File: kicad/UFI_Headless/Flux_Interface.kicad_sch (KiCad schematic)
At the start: 14 parts, among them U6 SN74LS07D, U7 SN74LS07D, U8 74LVC14AD

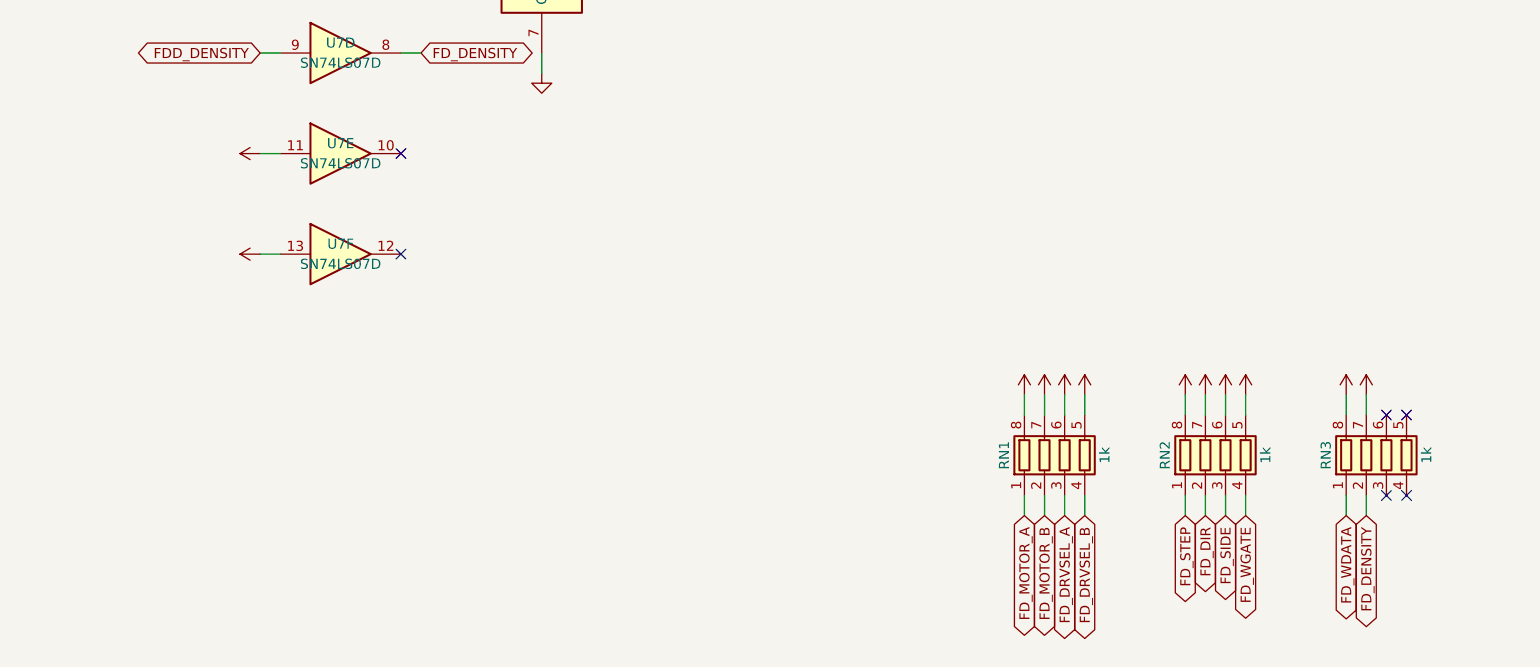
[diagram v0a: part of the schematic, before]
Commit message: UFI Headless v0.4: J6 pin 6 DRATE via JP1, pin 3 GND/+5V via JP2
DRATE is driven by PF11 through the spare LS07 gate U7.11 -> U7.10 with
pull-up RN3.3; J6 pin 6 only sees it when solder jumper JP1 is bridged.
J6 pin 3 goes through JP2 (default 1-2 = GND, 2-3 = FDD_5V for PS/2 drives).
Firmware moves FDD_DRATE from PE6 to PF11.
DRC 0 violations, 0 unconnected, parity clean; fab outputs regenerated.
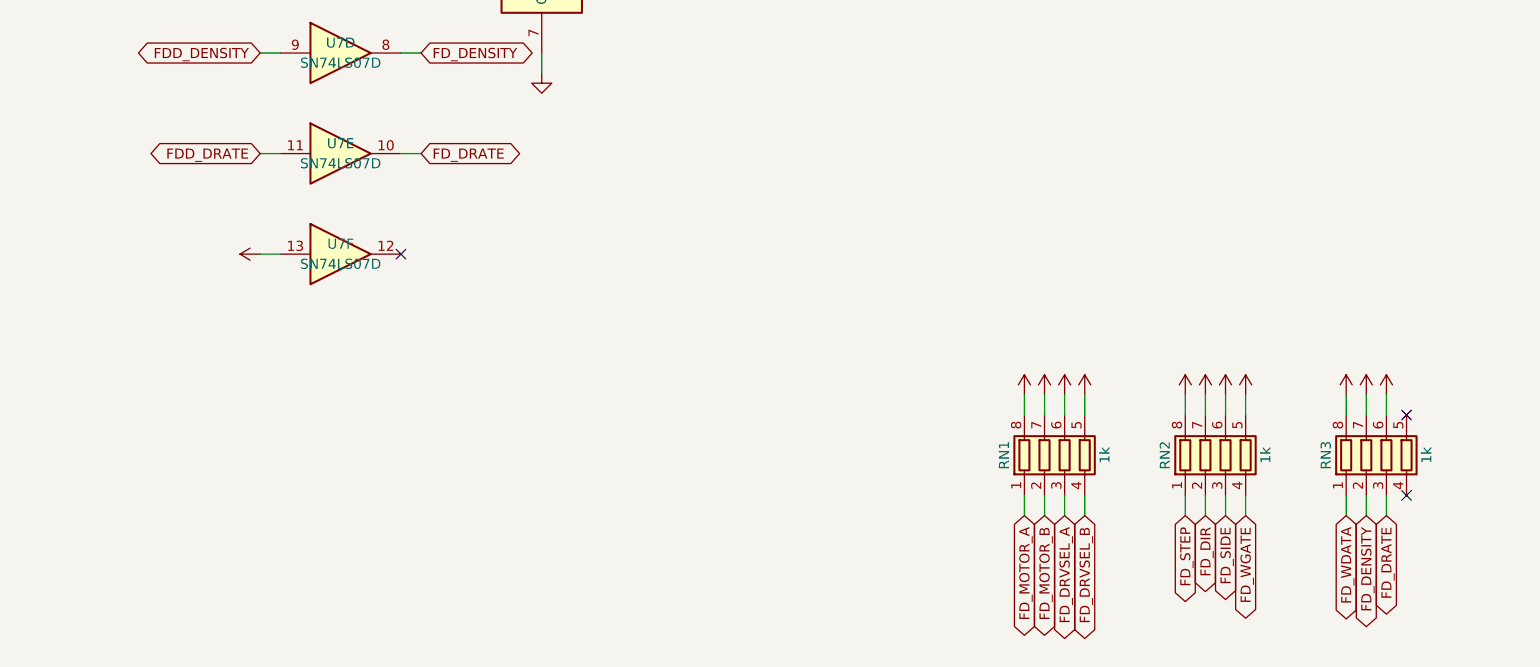
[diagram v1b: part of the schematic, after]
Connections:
- net +5V: now also RN3.6 (R3.2); no longer U7.11
- net FD_DRATE: now reaches RN3.3 (R3.1)
- net FD_DRATE: now also U7.10
- new net FDD_DRATE: U7.11
- no-connect marks 10 -> 7

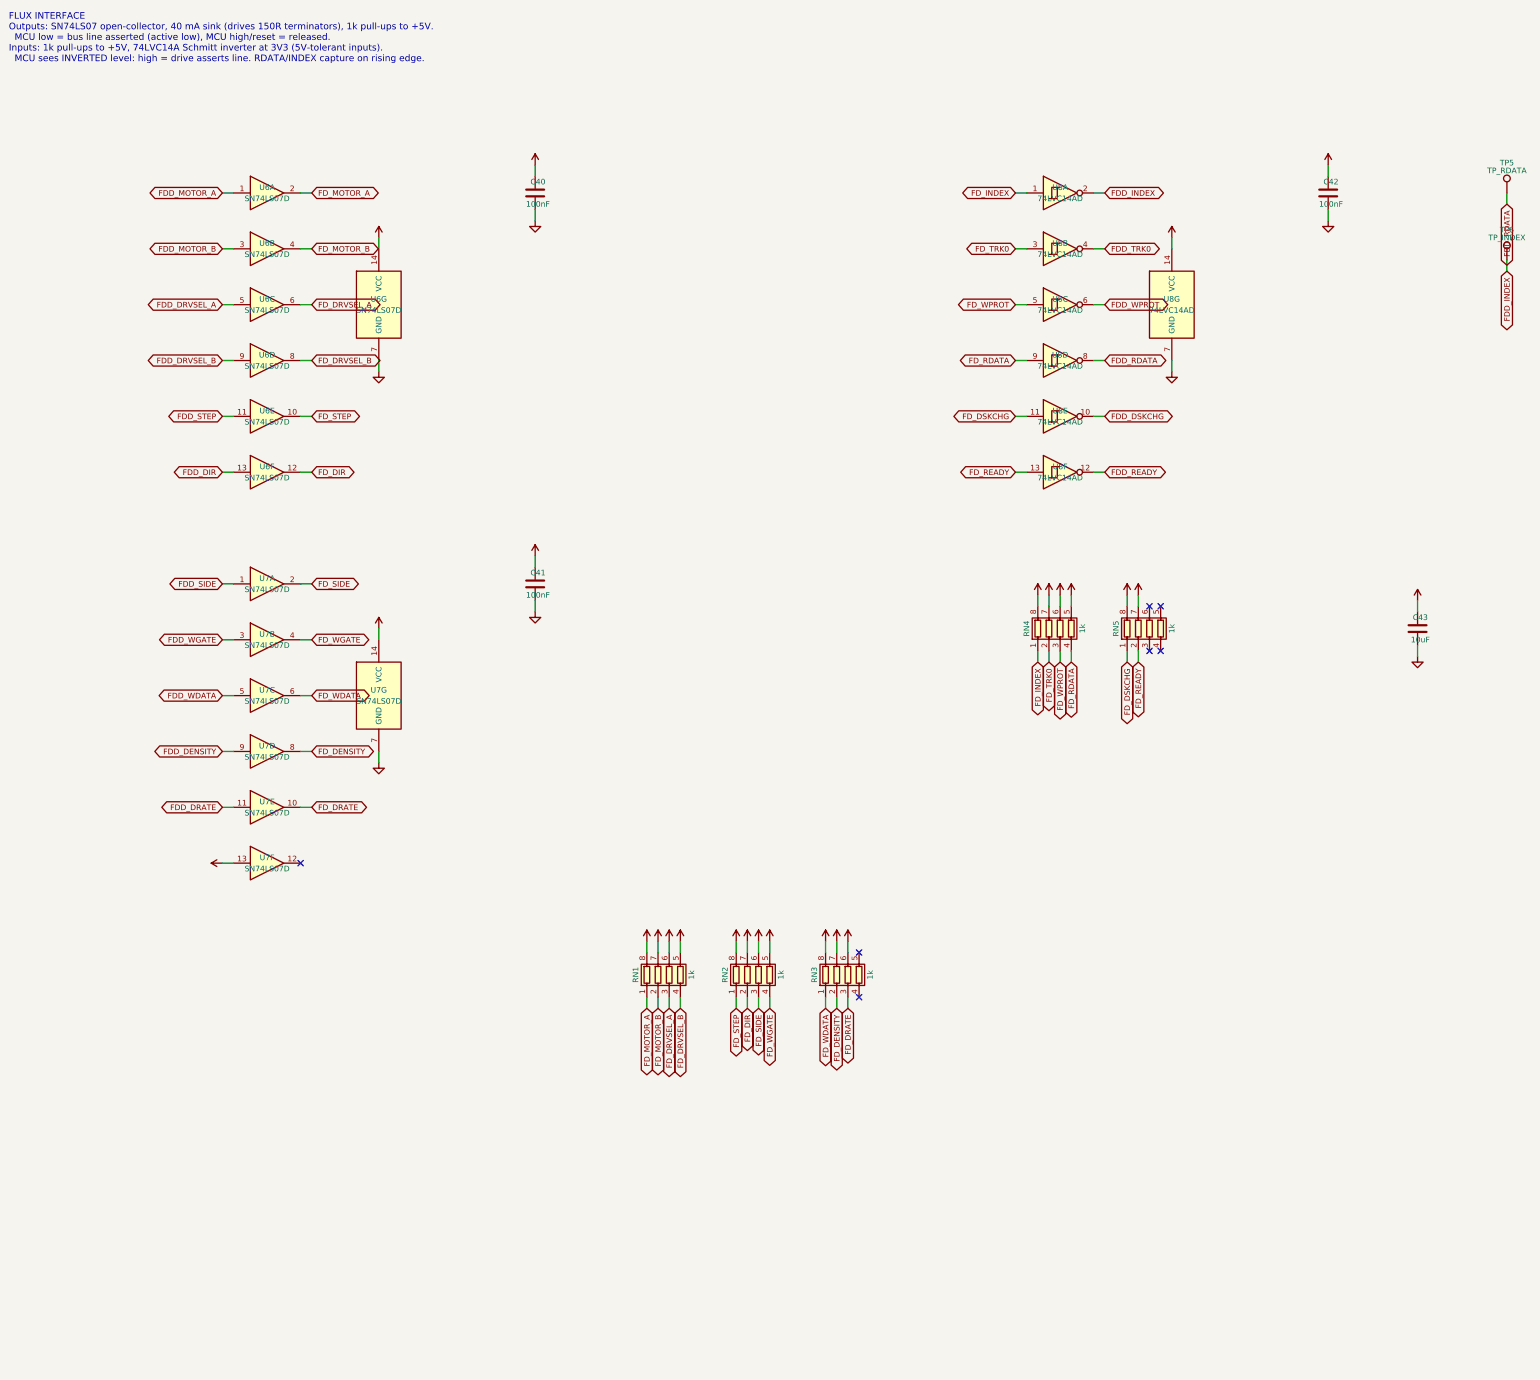
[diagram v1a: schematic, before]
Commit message: UFI Headless v0.5: switched/measured drive supplies, write lock, microSD, expansion
Hardware (A1-A9): FDD_5V/FDD_12V high-side P-FET switches (off in reset)
with 0.1R + INA180A1 current sense, TVS at both outputs; WRITE LOCK
jumper J11 gates WGATE through 74LVC1G32 (TP8 now shows the gated
signal); expansion header J9 (I2C1, 2 GPIO, button lines, 3V3/5V),
buttons SW3/SW4; microSD J10 on SDMMC2 with the card slot facing the
top edge; board ID divider on PA4; test points TP7/TP8.  12V reverse
protection already existed; 8-inch 50-pin port left out (board size).
ECO placed 37 parts; Freerouting plus hand routes for the rest.
New scripts/eco/ tools (maze router, route check, cluster/occupancy
maps, via scan), add_silk_label.py no longer crashes on re-placement.
ERC 0, DRC 0 incl. warnings, 0 unconnected, parity clean, no via-in-pad;
fab outputs regenerated (146 CPL rows).
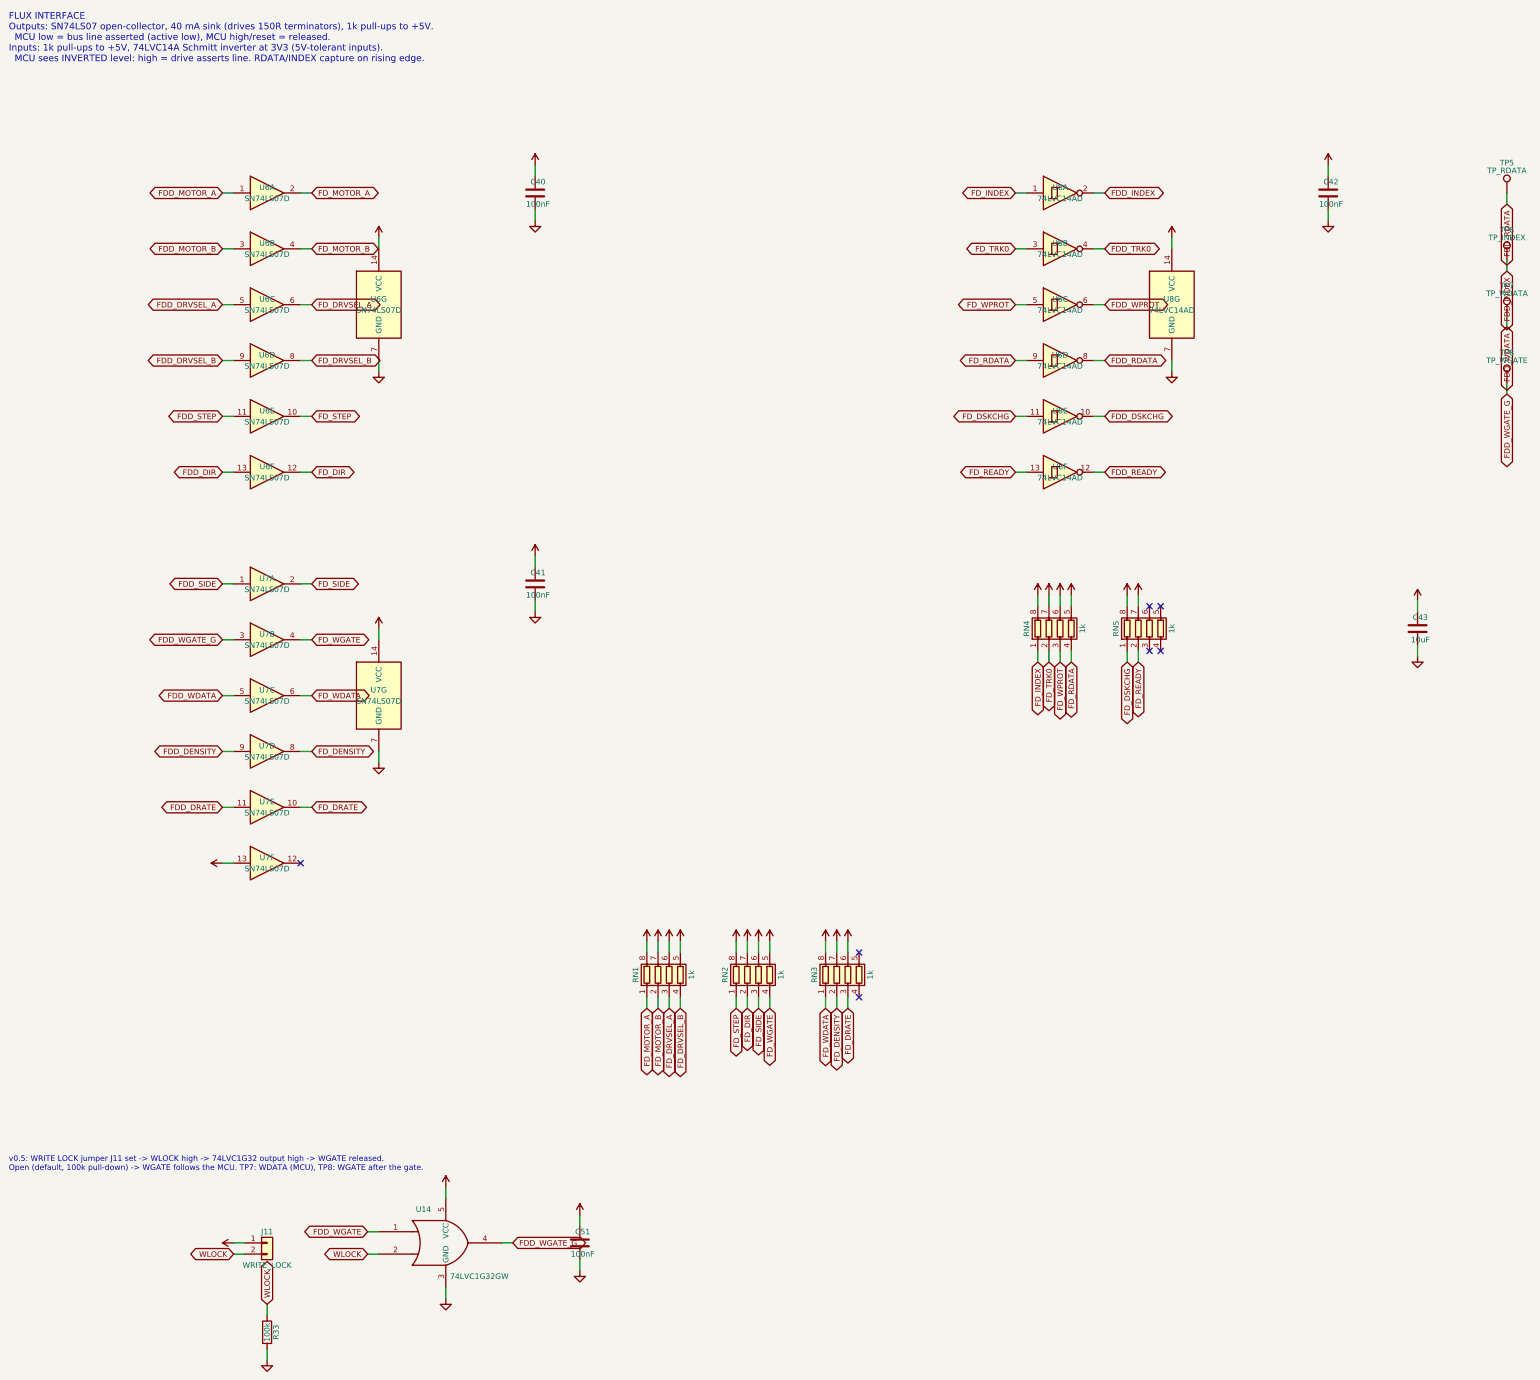
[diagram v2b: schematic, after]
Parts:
- added C51: 100nF, Capacitor_SMD:C_0603_1608Metric, symbol Device:C
- added J11: WRITE_LOCK, Connector_PinHeader_2.54mm:PinHeader_1x02_P2.54mm_Vertical, symbol Connector_Generic:Conn_01x02
- added R33: 100k, Resistor_SMD:R_0603_1608Metric, symbol Device:R
- added TP7: TP_WDATA, TestPoint:TestPoint_Pad_D1.5mm, symbol Connector:TestPoint
- added TP8: TP_WGATE, TestPoint:TestPoint_Pad_D1.5mm, symbol Connector:TestPoint
- added U14: 74LVC1G32GW, Package_TO_SOT_SMD:SOT-353_SC-70-5, symbol 74xGxx:74LVC1G32
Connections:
- net +3V3: now also C51.1, J11.1 (Pin_1), U14.5 (VCC)
- net FDD_WDATA: now also TP7.1
- net FDD_WGATE: now also U14.1; no longer U7.3
- net GND: now also C51.2, R33.2, U14.3 (GND)
- new net FDD_WGATE_G: TP8.1, U14.4, U7.3
- new net WLOCK: J11.2 (Pin_2), R33.1, U14.2
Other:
- note added: "v0.5: WRITE LOCK jumper J11 set -> WLOCK high -> 74LVC1G32 output high -> WGATE released. Open (default, 100k pull-down) -> WGATE follows the MCU. TP7: WDATA (MCU), TP8: WGATE after the gate."
